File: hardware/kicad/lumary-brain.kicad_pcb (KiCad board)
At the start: 4 copper layers, 62.3 x 30.3 mm, 32 parts, among them J1 PWR_IN, J2 CN1, J3 USB-C, Q1 NMOS_60V, Q2 NMOS_60V, Q3 AO3401A, SW1 BOOT, SW2 EN, U1 ESP32-H2-MINI-1-N4, U2 ME6211C33M5G, U3 74AHCT1G125, U4 USBLC6-2SC6

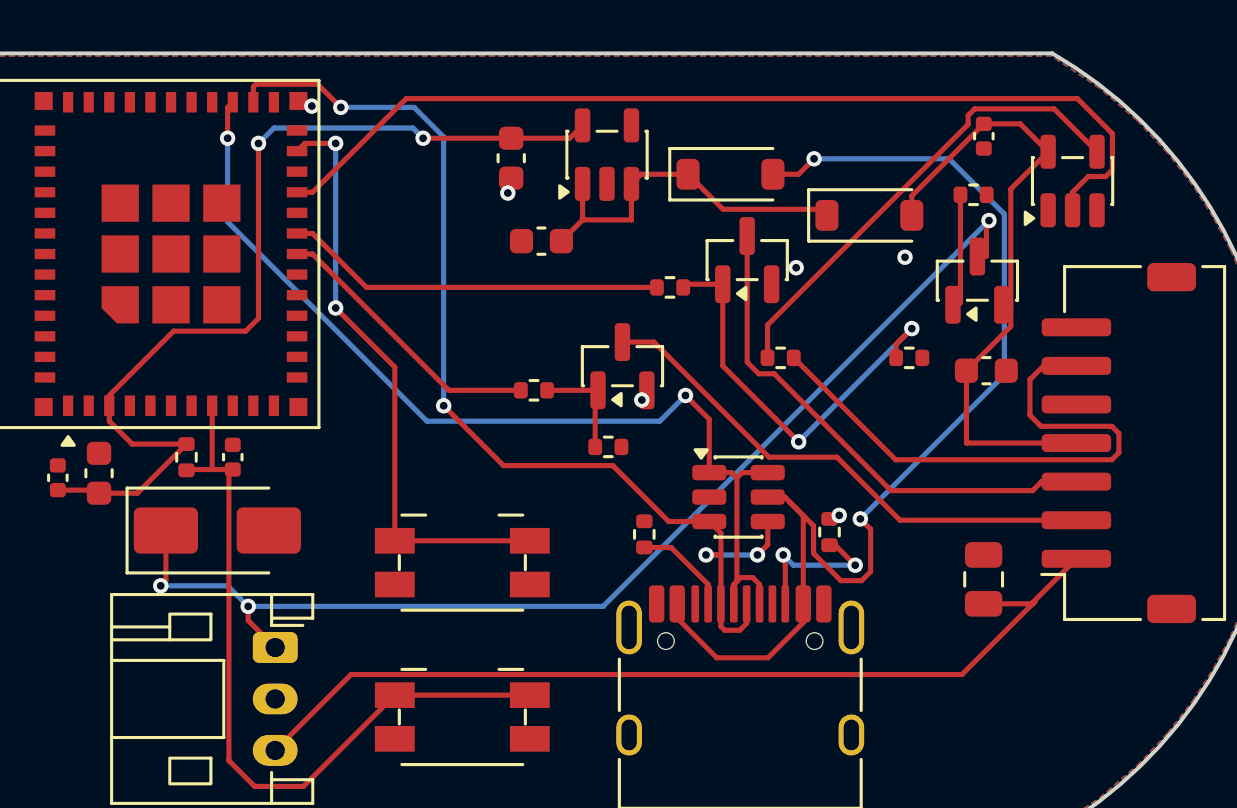
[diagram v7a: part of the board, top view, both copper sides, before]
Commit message: feat: power widening where it pays, 2-layer stackup, silkscreen
Widening: +4V7 and +4V7_IN keep 0.5mm -- they are the only nets that can
exceed the 0.74A a 0.2mm track supports. +36V, CW_RET and WW_RET carry 380mA
fixed by the CC driver; +3V3, VBUS and LDO_IN are module rails. All six went
back to 0.2mm, which removed 25 of the 28 clearance violations the blanket
widening caused.

Three short necks stay at 0.2mm, recorded by segment id: two on +4V7 where it
threads between C7's ground pad and RING_BUF_OUT, and a 1.5mm stub on +4V7_IN
past J3's shield pad. Be clear about what that means: the ring supply path's
limit is still ~0.74A. The widening did not raise it -- it cut about 60
milliohms, some 35mV at the 0.55A this actually draws. Clearing the necks
needs RING_BUF_OUT rerouted out of that corner, which is a design change.

Antenna keepout now reaches the bottom board edge. The 1mm shrink had left a
0.9mm strip under the antenna where the pour could fill.

Stackup drops from 4 copper layers to 2. In1.Cu and In2.Cu carried no routing
at all -- only ground pours -- while every document called this a two-layer
board.

kicad-cli DRC: 0 violations, 0 unconnected.

Co-Authored-By: Claude Opus 5 <noreply@anthropic.com>
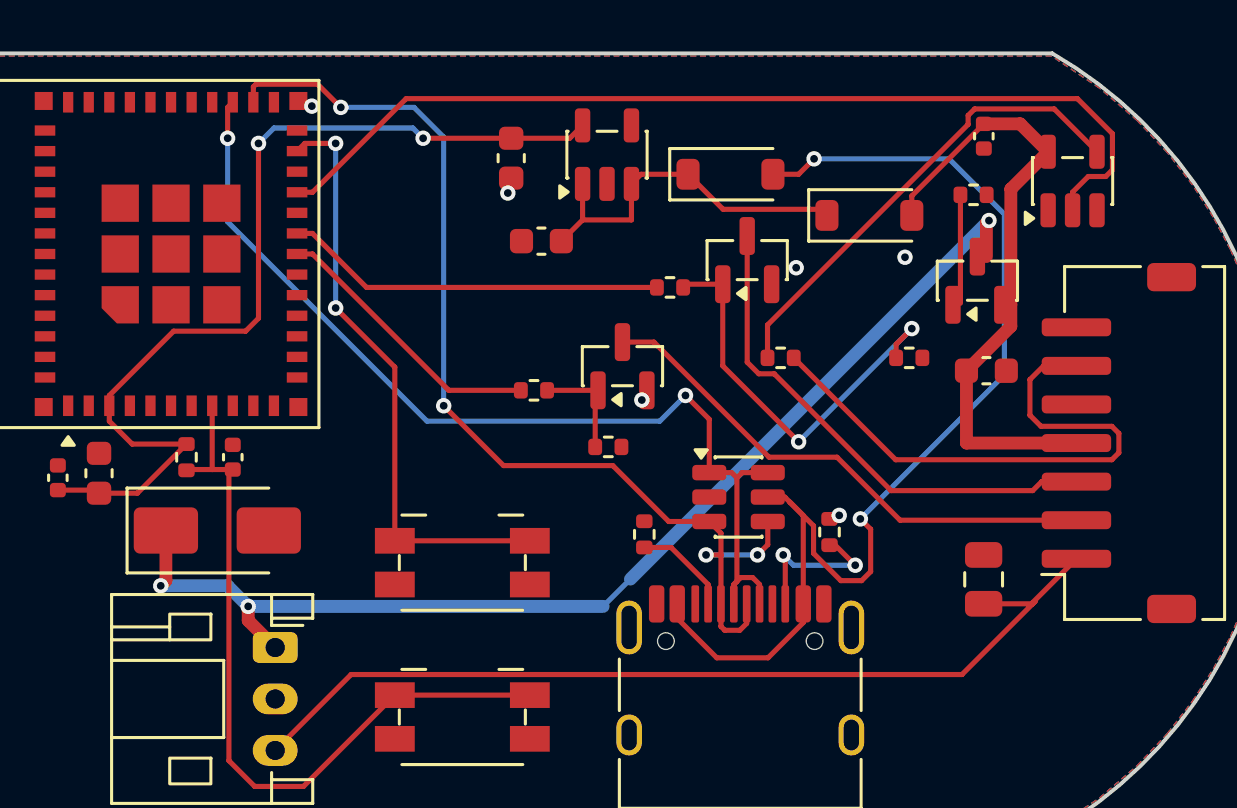
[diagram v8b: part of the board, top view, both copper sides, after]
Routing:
- removed copper zone on In1.Cu, net GND
- removed copper zone on In2.Cu, net GND
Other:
- copper layers 4 -> 2
- board text added: "Chad Michaud 2026"
- board text added: "Lumary Brain rev B"
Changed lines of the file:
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@@
 	(layers
 		(0 "F.Cu" signal)
-		(4 "In1.Cu" signal)
-		(6 "In2.Cu" signal)
 		(2 "B.Cu" signal)
 		(9 "F.Adhes" user "F.Adhesive")
@@
 		)
 		(zone
-			(layers "F.Cu" "B.Cu" "In1.Cu" "In2.Cu")
+			(layers "F.Cu" "B.Cu")
 			(name "Antenna")
 			(hatch full 0.508)
@@
 			(polygon
 				(pts
-					(xy 131.807447 67.8) (xy 131.807447 111) (xy 111.407447 111) (xy 111.407447 67.8)
+					(xy 131.807447 67.8) (xy 131.807447 112.5) (xy 111.407447 112.5) (xy 111.407447 67.8)
 				)
 			)
@@
 		(start 170.057447 86.875)
 		(end 170.057447 91.375)
-		(width 0.2)
+		(width 0.5)
 		(layer "F.Cu")
 		(net "+4V7")
@@
 		(start 168.332447 96.75)
 		(end 168.332447 93.9375)
-		(width 0.2)
+		(width 0.5)
 		(layer "F.Cu")
 		(net "+4V7")
@@
 		(start 170.422447 84.34)
 		(end 169.007447 84.34)
-		(width 0.2)
+		(width 0.5)
 		(layer "F.Cu")
 		(net "+4V7")
@@
 		(start 170.057447 92.2125)
 		(end 168.332447 93.9375)
-		(width 0.2)
+		(width 0.5)
 		(layer "F.Cu")
 		(net "+4V7")
@@
 		(start 170.057447 91.375)
 		(end 170.057447 92.2125)
-		(width 0.2)
+		(width 0.5)
 		(layer "F.Cu")
 		(net "+4V7")
@@
 		(start 171.507447 85.425)
 		(end 170.422447 84.34)
-		(width 0.2)
+		(width 0.5)
 		(layer "F.Cu")
 		(net "+4V7")
@@
 		(start 172.607447 96.75)
 		(end 168.332447 96.75)
-		(width 0.2)
+		(width 0.5)
 		(layer "F.Cu")
 		(net "+4V7")
@@
 		(start 171.507447 85.425)
 		(end 170.057447 86.875)
-		(width 0.2)
+		(width 0.5)
 		(layer "F.Cu")
 		(net "+4V7")
@@
 		(start 141.457447 104.7)
 		(end 140.407447 103.65)
-		(width 0.2)
+		(width 0.5)
 		(layer "F.Cu")
 		(net "+4V7_IN")
@@
 		(start 140.407447 103.65)
 		(end 140.407447 103.1)
-		(width 0.2)
+		(width 0.5)
 		(layer "F.Cu")
 		(net "+4V7_IN")
@@
 		(start 169.107447 89.5)
 		(end 169.107447 88.2)
-		(width 0.2)
+		(width 0.5)
 		(layer "F.Cu")
 		(net "+4V7_IN")
@@
 		(start 137.207447 102.1)
 		(end 137.207447 100.15)
-		(width 0.2)
+		(width 0.5)
 		(layer "F.Cu")
 		(net "+4V7_IN")
@@
 		(start 137.007447 102.3)
 		(end 137.207447 102.1)
-		(width 0.2)
+		(width 0.5)
 		(layer "F.Cu")
 		(net "+4V7_IN")
@@
 		(start 169.107447 88.2)
 		(end 169.207447 88.1)
-		(width 0.2)
+		(width 0.5)
 		(layer "F.Cu")
 		(net "+4V7_IN")
@@
 		(start 140.407447 103.1)
 		(end 139.607447 102.3)
-		(width 0.2)
+		(width 0.5)
 		(layer "B.Cu")
 		(net "+4V7_IN")
@@
 	(segment
 		(start 169.207447 88.1)
-		(end 154.207447 103.1)
-		(width 0.2)
+		(end 155.268107 102.03934)
+		(width 0.5)
 		(layer "B.Cu")
 		(net "+4V7_IN")
@@
 		(start 139.607447 102.3)
 		(end 137.007447 102.3)
+		(width 0.5)
+		(layer "B.Cu")
+		(net "+4V7_IN")
+	)
+	(segment
+		(start 155.268107 102.03934)
+		(end 154.207447 103.1)
 		(width 0.2)
 		(layer "B.Cu")
@@
 		(start 154.207447 103.1)
 		(end 140.407447 103.1)
-		(width 0.2)
+		(width 0.5)
 		(layer "B.Cu")
 		(net "+4V7_IN")
@@
 	)
 	(segment
-		(start 170.907447 102.95)
-		(end 172.607447 101.25)
-		(width 0.2)
-		(layer "F.Cu")
-		(net "+36V")
-	)
-	(segment
-		(start 170.907447 103)
-		(end 171.007447 102.9)
-		(width 0.2)
-		(layer "F.Cu")
-		(net "+36V")
-	)
-	(segment
-		(start 144.407447 105.75)
-		(end 141.457447 108.7)
-		(width 0.2)
-		(layer "F.Cu")
-		(net "+36V")
-	)
-	(segment
-		(start 170.907447 103)
-		(end 170.907447 102.95)
+		(start 168.097447 87.1)
+		(end 168.097447 91.315)
 		(width 0.2)
 		(layer "F.Cu")
-		(net "+36V")
+		(net "Q3_GATE")
 	)
 	(segment
-		(start 171.007447 102.9)
-		(end 168.157447 105.75)
+		(start 152.027447 94.7)
+		(end 154.007447 94.7)
 		(width 0.2)
 		(layer "F.Cu")
-		(net "+36V")
+		(net "CW_GATE")
 	)
 	(segment
-		(start 168.157447 105.75)
-		(end 144.407447 105.75)
+		(start 153.897447 94.81)
+		(end 154.007447 94.7)
 		(width 0.2)
 		(layer "F.Cu")
-		(net "+36V")
+		(net "CW_GATE")
 	)
 	(segment
-		(start 169 103)
-		(end 170.907447 103)
+		(start 153.897447 96.9)
+		(end 153.897447 94.81)
 		(width 0.2)
 		(layer "F.Cu")
-		(net "+36V")
+		(net "CW_GATE")
 	)
 	(segment
@@
 	)
 	(segment
+		(start 170.907447 102.95)
+		(end 172.607447 101.25)
+		(width 0.2)
+		(layer "F.Cu")
+		(net "+36V")
+	)
+	(segment
+		(start 170.907447 103)
+		(end 171.007447 102.9)
+		(width 0.2)
+		(layer "F.Cu")
+		(net "+36V")
+	)
+	(segment
+		(start 144.407447 105.75)
+		(end 141.457447 108.7)
+		(width 0.2)
+		(layer "F.Cu")
+		(net "+36V")
+	)
+	(segment
+		(start 170.907447 103)
+		(end 170.907447 102.95)
+		(width 0.2)
+		(layer "F.Cu")
+		(net "+36V")
+	)
+	(segment
+		(start 171.007447 102.9)
+		(end 168.157447 105.75)
+		(width 0.2)
+		(layer "F.Cu")
+		(net "+36V")
+	)
+	(segment
+		(start 168.157447 105.75)
+		(end 144.407447 105.75)
+		(width 0.2)
+		(layer "F.Cu")
+		(net "+36V")
+	)
+	(segment
+		(start 169 103)
+		(end 170.907447 103)
+		(width 0.2)
+		(layer "F.Cu")
+		(net "+36V")
+	)
+	(segment
 		(start 160.8575 94.0575)
 		(end 165.4 98.6)
@@
 	)
 	(segment
-		(start 168.097447 87.1)
-		(end 168.097447 91.315)
-		(width 0.2)
-		(layer "F.Cu")
-		(net "Q3_GATE")
-	)
-	(segment
-		(start 152.027447 94.7)
-		(end 154.007447 94.7)
-		(width 0.2)
-		(layer "F.Cu")
-		(net "CW_GATE")
-	)
-	(segment
-		(start 153.897447 94.81)
-		(end 154.007447 94.7)
-		(width 0.2)
-		(layer "F.Cu")
-		(net "CW_GATE")
-	)
-	(segment
-		(start 153.897447 96.9)
-		(end 153.897447 94.81)
-		(width 0.2)
-		(layer "F.Cu")
-		(net "CW_GATE")
-	)
-	(segment
 		(start 161.287447 103.005)
 		(end 161.287447 101.18)
@@
 		)
 	)
-	(zone
-		(net "GND")
-		(layer "In1.Cu")
-		(name "GND_In1.Cu")
-		(hatch edge 0.5)
-		(connect_pads yes
-			(clearance 0.3)
-		)
-		(min_thickness 0.25)
-		(fill yes
-			(thermal_gap 0.5)
-			(thermal_bridge_width 0.5)
-			(island_removal_mode 0)
-		)
-		(polygon
-			(pts
-				(xy 126.874892 81.7) (xy 125.00391 82.954166) (xy 123.546493 84.208333) (xy 122.365379 85.4625)
-				(xy 121.391532 86.716666) (xy 120.584589 87.970833) (xy 119.918776 89.225) (xy 119.376715 90.479166)
-				(xy 118.946322 91.733333) (xy 118.61911 92.9875) (xy 118.389193 94.241666) (xy 118.252705 95.495833)
-				(xy 118.207447 96.75) (xy 118.252705 98.004166) (xy 118.389193 99.258333) (xy 118.61911 100.5125)
-				(xy 118.946322 101.766666) (xy 119.376715 103.020833) (xy 119.918776 104.275) (xy 120.584589 105.529166)
-				(xy 121.391532 106.783333) (xy 122.365379 108.0375) (xy 123.546493 109.291666) (xy 125.00391 110.545833)
-				(xy 126.874892 111.8) (xy 171.640001 111.8) (xy 173.510983 110.545833) (xy 174.9684 109.291666)
-				(xy 176.149514 108.0375) (xy 177.123361 106.783333) (xy 177.930304 105.529166) (xy 178.596117 104.275)
-				(xy 179.138178 103.020833) (xy 179.568571 101.766666) (xy 179.895783 100.5125) (xy 180.1257 99.258333)
-				(xy 180.262188 98.004166) (xy 180.307446 96.75) (xy 180.262188 95.495833) (xy 180.1257 94.241666)
-				(xy 179.895783 92.9875) (xy 179.568571 91.733333) (xy 179.138178 90.479166) (xy 178.596117 89.225)
-				(xy 177.930304 87.970833) (xy 177.123361 86.716666) (xy 176.149514 85.4625) (xy 174.9684 84.208333)
-				(xy 173.510983 82.954166) (xy 171.640001 81.7)
-			)
-		)
-	)
-	(zone
-		(net "GND")
-		(layer "In2.Cu")
-		(name "GND_In2.Cu")
-		(hatch edge 0.5)
-		(connect_pads yes
-			(clearance 0.3)
-		)
-		(min_thickness 0.25)
-		(fill yes
-			(thermal_gap 0.5)
-			(thermal_bridge_width 0.5)
-			(island_removal_mode 0)
-		)
-		(polygon
-			(pts
-				(xy 126.874892 81.7) (xy 125.00391 82.954166) (xy 123.546493 84.208333) (xy 122.365379 85.4625)
-				(xy 121.391532 86.716666) (xy 120.584589 87.970833) (xy 119.918776 89.225) (xy 119.376715 90.479166)
-				(xy 118.946322 91.733333) (xy 118.61911 92.9875) (xy 118.389193 94.241666) (xy 118.252705 95.495833)
-				(xy 118.207447 96.75) (xy 118.252705 98.004166) (xy 118.389193 99.258333) (xy 118.61911 100.5125)
-				(xy 118.946322 101.766666) (xy 119.376715 103.020833) (xy 119.918776 104.275) (xy 120.584589 105.529166)
-				(xy 121.391532 106.783333) (xy 122.365379 108.0375) (xy 123.546493 109.291666) (xy 125.00391 110.545833)
-				(xy 126.874892 111.8) (xy 171.640001 111.8) (xy 173.510983 110.545833) (xy 174.9684 109.291666)
-				(xy 176.149514 108.0375) (xy 177.123361 106.783333) (xy 177.930304 105.529166) (xy 178.596117 104.275)
-				(xy 179.138178 103.020833) (xy 179.568571 101.766666) (xy 179.895783 100.5125) (xy 180.1257 99.258333)
-				(xy 180.262188 98.004166) (xy 180.307446 96.75) (xy 180.262188 95.495833) (xy 180.1257 94.241666)
-				(xy 179.895783 92.9875) (xy 179.568571 91.733333) (xy 179.138178 90.479166) (xy 178.596117 89.225)
-				(xy 177.930304 87.970833) (xy 177.123361 86.716666) (xy 176.149514 85.4625) (xy 174.9684 84.208333)
-				(xy 173.510983 82.954166) (xy 171.640001 81.7)
+	(embedded_fonts no)
+	(gr_text "Lumary Brain rev B"
+		(at 149.0 94.6 0)
+		(layer "B.SilkS")
+		(effects
+			(font
+				(size 1.2 1.2)
+				(thickness 0.2)
+			)
+			(justify mirror)
+		)
+	)
+	(gr_text "Chad Michaud 2026"
+		(at 149.0 96.8 0)
+		(layer "B.SilkS")
+		(effects
+			(font
+				(size 1.0 1.0)
+				(thickness 0.15)
 			)
+			(justify mirror)
 		)
 	)
-	(embedded_fonts no)
 )
